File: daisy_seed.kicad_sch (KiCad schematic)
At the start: 23 parts, among them J2 GPIO Header, J3 Micro_SD_Card, U3 Daisy_Seed, U4 H11L1SM

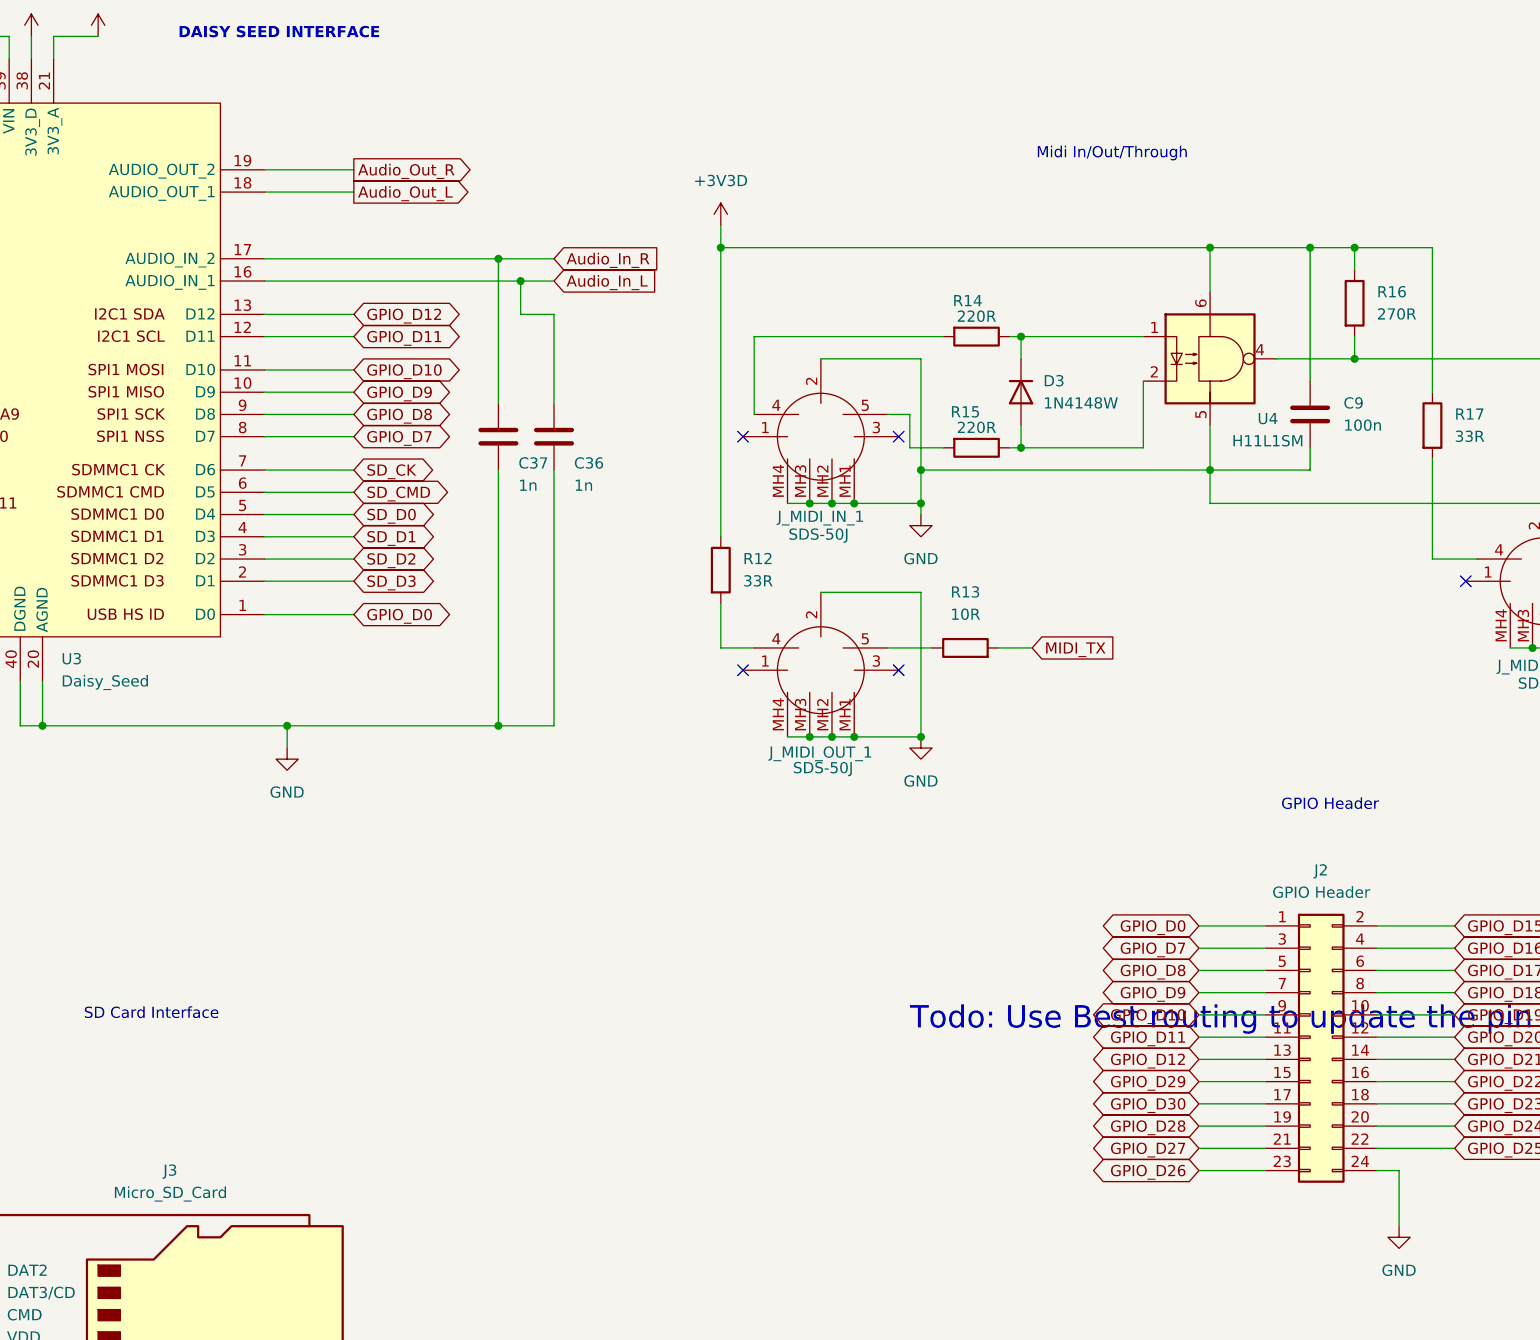
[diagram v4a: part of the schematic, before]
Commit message: fix some footprints
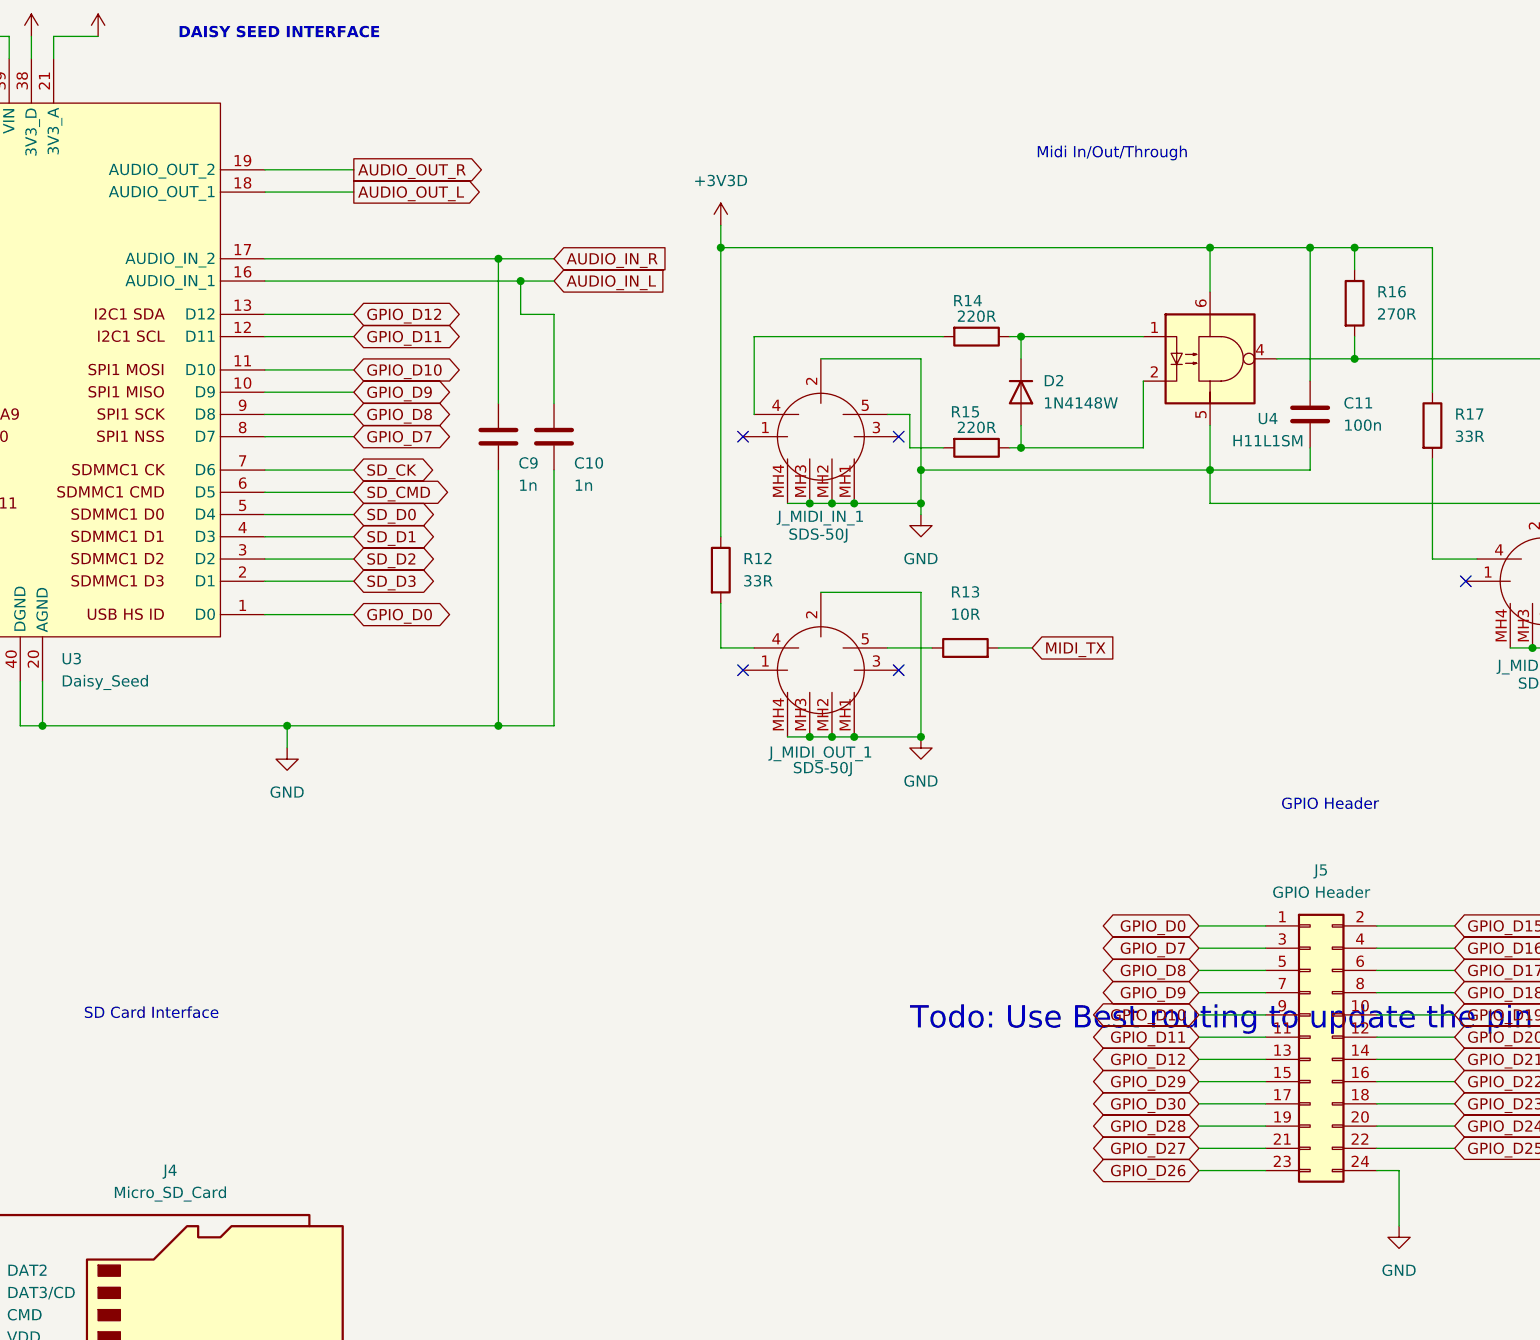
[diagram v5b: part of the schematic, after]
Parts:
- renumbered C36 to C10, C9 to C11, C37 to C9, D3 to D2, J3 to J4, J2 to J5
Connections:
- net Audio_In_L renamed AUDIO_IN_L
- net Audio_In_R renamed AUDIO_IN_R
- net Audio_Out_L renamed AUDIO_OUT_L
- net Audio_Out_R renamed AUDIO_OUT_R
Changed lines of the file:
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@@
 		)
 	)
-	(global_label "Audio_In_L"
+	(global_label "AUDIO_IN_L"
 		(shape input)
 		(at 128.27 52.07 0)
@@
 		)
 		(property "Intersheetrefs" "${INTERSHEET_REFS}"
-			(at 141.1127 52.07 0)
+			(at 141.7782 52.07 0)
 			(effects
 				(font
@@
 		)
 	)
-	(global_label "Audio_Out_L"
+	(global_label "AUDIO_OUT_L"
 		(shape output)
 		(at 105.41 41.91 0)
@@
 		)
 		(property "Intersheetrefs" "${INTERSHEET_REFS}"
-			(at 119.7041 41.91 0)
+			(at 120.6115 41.91 0)
 			(effects
 				(font
@@
 		)
 	)
-	(global_label "Audio_Out_R"
+	(global_label "AUDIO_OUT_R"
 		(shape output)
 		(at 105.41 39.37 0)
@@
 		)
 		(property "Intersheetrefs" "${INTERSHEET_REFS}"
-			(at 119.946 39.37 0)
+			(at 120.8534 39.37 0)
 			(effects
 				(font
@@
 		)
 	)
-	(global_label "Audio_In_R"
+	(global_label "AUDIO_IN_R"
 		(shape input)
 		(at 128.27 49.53 0)
@@
 		)
 		(property "Intersheetrefs" "${INTERSHEET_REFS}"
-			(at 141.3546 49.53 0)
+			(at 142.0201 49.53 0)
 			(effects
 				(font
@@
 		(dnp no)
 		(fields_autoplaced yes)
-		(property "Reference" "#PWR017"
+		(property "Reference" "#PWR027"
 			(at 224.79 166.37 0)
 			(effects
@@
 			(project "triptech"
 				(path "/55cca6a8-30da-4c13-b2f2-a01401e2b54c/75aee282-6ddd-4543-b5fc-0fc86bf548ec"
-					(reference "#PWR017")
+					(reference "#PWR027")
 					(unit 1)
 				)
@@
 		(dnp no)
 		(fields_autoplaced yes)
-		(property "Reference" "#PWR024"
+		(property "Reference" "#PWR025"
 			(at 170.18 85.09 0)
 			(effects
@@
 			(project "triptech"
 				(path "/55cca6a8-30da-4c13-b2f2-a01401e2b54c/75aee282-6ddd-4543-b5fc-0fc86bf548ec"
-					(reference "#PWR024")
+					(reference "#PWR025")
 					(unit 1)
 				)
@@
 		(dnp no)
 		(fields_autoplaced yes)
-		(property "Reference" "#PWR022"
+		(property "Reference" "#PWR024"
 			(at 147.32 49.53 0)
 			(effects
@@
 			(project ""
 				(path "/55cca6a8-30da-4c13-b2f2-a01401e2b54c/75aee282-6ddd-4543-b5fc-0fc86bf548ec"
-					(reference "#PWR022")
+					(reference "#PWR024")
 					(unit 1)
 				)
@@
 		(dnp no)
 		(fields_autoplaced yes)
-		(property "Reference" "#PWR019"
+		(property "Reference" "#PWR022"
 			(at 97.79 111.76 0)
 			(effects
@@
 			(project ""
 				(path "/55cca6a8-30da-4c13-b2f2-a01401e2b54c/75aee282-6ddd-4543-b5fc-0fc86bf548ec"
-					(reference "#PWR019")
+					(reference "#PWR022")
 					(unit 1)
 				)
@@
 		(dnp no)
 		(fields_autoplaced yes)
-		(property "Reference" "C9"
+		(property "Reference" "C11"
 			(at 218.44 66.0399 0)
 			(effects
@@
 			(project ""
 				(path "/55cca6a8-30da-4c13-b2f2-a01401e2b54c/75aee282-6ddd-4543-b5fc-0fc86bf548ec"
-					(reference "C9")
+					(reference "C11")
 					(unit 1)
 				)
@@
 		(on_board yes)
 		(dnp no)
-		(property "Reference" "C36"
+		(property "Reference" "C10"
 			(at 130.556 72.898 0)
 			(effects
@@
 			(project ""
 				(path "/55cca6a8-30da-4c13-b2f2-a01401e2b54c/75aee282-6ddd-4543-b5fc-0fc86bf548ec"
-					(reference "C36")
+					(reference "C10")
 					(unit 1)
 				)
@@
 		(dnp no)
 		(fields_autoplaced yes)
-		(property "Reference" "#PWR018"
+		(property "Reference" "#PWR020"
 			(at 68.58 27.94 0)
 			(effects
@@
 			(project ""
 				(path "/55cca6a8-30da-4c13-b2f2-a01401e2b54c/75aee282-6ddd-4543-b5fc-0fc86bf548ec"
-					(reference "#PWR018")
+					(reference "#PWR020")
 					(unit 1)
 				)
@@
 		(on_board yes)
 		(dnp no)
-		(property "Reference" "C37"
+		(property "Reference" "C9"
 			(at 124.206 72.898 0)
 			(effects
@@
 			(project "daisy-studio"
 				(path "/55cca6a8-30da-4c13-b2f2-a01401e2b54c/75aee282-6ddd-4543-b5fc-0fc86bf548ec"
-					(reference "C37")
+					(reference "C9")
 					(unit 1)
 				)
@@
 		(dnp no)
 		(fields_autoplaced yes)
-		(property "Reference" "#PWR026"
+		(property "Reference" "#PWR028"
 			(at 251.46 111.76 0)
 			(effects
@@
 			(project "triptech"
 				(path "/55cca6a8-30da-4c13-b2f2-a01401e2b54c/75aee282-6ddd-4543-b5fc-0fc86bf548ec"
-					(reference "#PWR026")
+					(reference "#PWR028")
 					(unit 1)
 				)
@@
 		(dnp no)
 		(fields_autoplaced yes)
-		(property "Reference" "#PWR025"
+		(property "Reference" "#PWR026"
 			(at 170.18 110.49 0)
 			(effects
@@
 			(project "triptech"
 				(path "/55cca6a8-30da-4c13-b2f2-a01401e2b54c/75aee282-6ddd-4543-b5fc-0fc86bf548ec"
-					(reference "#PWR025")
+					(reference "#PWR026")
 					(unit 1)
 				)
@@
 		(on_board yes)
 		(dnp no)
-		(property "Reference" "J2"
+		(property "Reference" "J5"
 			(at 215.9 119.38 0)
 			(effects
@@
 			(project ""
 				(path "/55cca6a8-30da-4c13-b2f2-a01401e2b54c/75aee282-6ddd-4543-b5fc-0fc86bf548ec"
-					(reference "J2")
+					(reference "J5")
 					(unit 1)
 				)
@@
 		(dnp no)
 		(fields_autoplaced yes)
-		(property "Reference" "J3"
+		(property "Reference" "J4"
 			(at 84.455 153.67 0)
 			(effects
@@
 			(project ""
 				(path "/55cca6a8-30da-4c13-b2f2-a01401e2b54c/75aee282-6ddd-4543-b5fc-0fc86bf548ec"
-					(reference "J3")
+					(reference "J4")
 					(unit 1)
 				)
@@
 		(dnp no)
 		(fields_autoplaced yes)
-		(property "Reference" "#PWR021"
+		(property "Reference" "#PWR018"
 			(at 40.64 123.19 0)
 			(effects
@@
 			(project ""
 				(path "/55cca6a8-30da-4c13-b2f2-a01401e2b54c/75aee282-6ddd-4543-b5fc-0fc86bf548ec"
-					(reference "#PWR021")
+					(reference "#PWR018")
 					(unit 1)
 				)
@@
 		(dnp no)
 		(fields_autoplaced yes)
-		(property "Reference" "#PWR020"
+		(property "Reference" "#PWR021"
 			(at 76.2 27.94 0)
 			(effects
@@
 			(project ""
 				(path "/55cca6a8-30da-4c13-b2f2-a01401e2b54c/75aee282-6ddd-4543-b5fc-0fc86bf548ec"
-					(reference "#PWR020")
+					(reference "#PWR021")
 					(unit 1)
 				)
@@
 		(dnp no)
 		(fields_autoplaced yes)
-		(property "Reference" "D3"
+		(property "Reference" "D2"
 			(at 184.15 63.4999 90)
 			(effects
@@
 			(project ""
 				(path "/55cca6a8-30da-4c13-b2f2-a01401e2b54c/75aee282-6ddd-4543-b5fc-0fc86bf548ec"
-					(reference "D3")
+					(reference "D2")
 					(unit 1)
 				)
@@
 		(dnp no)
 		(fields_autoplaced yes)
-		(property "Reference" "#PWR016"
+		(property "Reference" "#PWR019"
 			(at 60.96 27.94 0)
 			(effects
@@
 			(project ""
 				(path "/55cca6a8-30da-4c13-b2f2-a01401e2b54c/75aee282-6ddd-4543-b5fc-0fc86bf548ec"
-					(reference "#PWR016")
+					(reference "#PWR019")
 					(unit 1)
 				)

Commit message: starting on output
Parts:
- C10, C9: value 1n -> C
- C11: value 100n -> C
- D2: value 1N4148W -> 1N4148WS; footprint Diode_SMD:D_SOD-123 -> Diode_SMD:D_SOD-323
- J5: value GPIO Header -> Conn_02x12_Odd_Even
- R10, R11, R7, R8, R9: value 47K -> R
- R12, R17, R18: value 33R -> R
- R13: value 10R -> R
- R14, R15: value 220R -> R
- R16: value 270R -> R
- U3: footprint daisy-studio:DAISY_SEED_SMT -> daisy-studio:DAISY_SEED
- U4: value H11L1SM -> H11L1
- renumbered J_MIDI_IN_1 to J1, J_MIDI_OUT_1 to J1, J_MIDI_THRU1 to J1
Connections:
- net GND: no longer J4.10 (Detect), J4.11 (SHIELD)

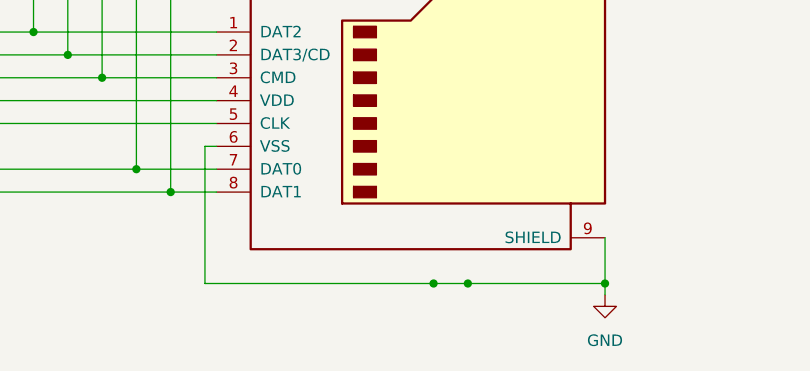
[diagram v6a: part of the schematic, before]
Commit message: daughterboard added
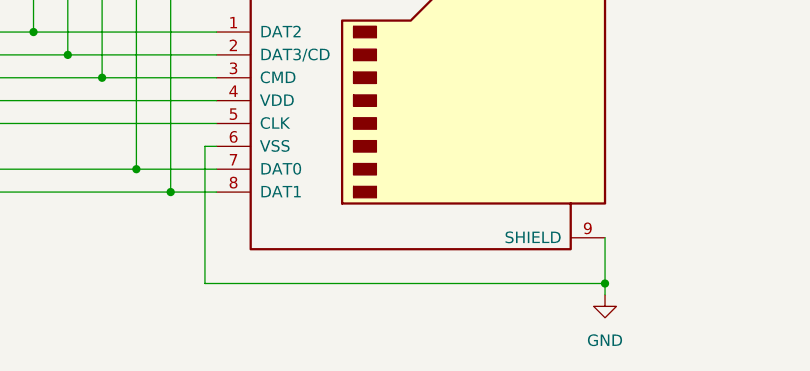
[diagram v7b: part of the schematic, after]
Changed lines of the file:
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@@
-	)
-	(junction
-		(at 85.09 193.04)
-		(diameter 0)
-		(color 0 0 0 0)
 	)
 	(junction
@@
 	(junction
 		(at 160.02 77.47)
-		(diameter 0)
-		(color 0 0 0 0)
-	)
-	(junction
-		(at 88.9 193.04)
 		(diameter 0)
 		(color 0 0 0 0)
@@
 	(wire
 		(pts
-			(xy 85.09 193.04) (xy 88.9 193.04)
-		)
-		(stroke
-			(width 0)
-			(type default)
-		)
-	)
-	(wire
-		(pts
 			(xy 34.29 167.64) (xy 44.45 167.64)
 		)
@@
 	(wire
 		(pts
-			(xy 88.9 193.04) (xy 104.14 193.04)
-		)
-		(stroke
-			(width 0)
-			(type default)
-		)
-	)
-	(wire
-		(pts
 			(xy 69.85 102.87) (xy 97.79 102.87)
 		)
@@
 	(wire
 		(pts
-			(xy 59.69 193.04) (xy 85.09 193.04)
-		)
-		(stroke
+			(xy 59.69 193.04) (xy 104.14 193.04)
+		)
+		(stroke
